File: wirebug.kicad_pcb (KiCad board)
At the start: 2 copper layers, 35 x 65 mm, 11 parts, among them J1 Screw_Terminal_01x02, J2 Screw_Terminal_01x02, J3 Screw_Terminal_01x02, K1 AW3211F, Q1 BC337, Q2 BC337

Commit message: RC1
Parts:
- added REF**: via_0.9, twyleg-misc:via_0.9, F.Cu at (120.9, 55.6)
- R1, R2: footprint Resistor_THT:R_Axial_DIN0204_L3.6mm_D1.6mm_P2.54mm_Vertical -> Resistor_THT:R_Axial_DIN0207_L6.3mm_D2.5mm_P2.54mm_Vertical
- moved Q1 2.72 mm to (110.9, 79.0), turned to -90 degrees
- moved Q2 2.68 mm to (117.9, 79.0), turned to -90 degrees
- moved PS1 2.55 mm to (121.3, 71.8)
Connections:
- A1 pad 13: unconnected-(A1-GND-Pad13) -> /GND
- A1 pad 18: unconnected-(A1-GND-Pad18) -> /GND
- A1 pad 23: unconnected-(A1-GND-Pad23) -> /GND
- A1 pad 28: unconnected-(A1-GND-Pad28) -> /GND
- A1 pad 3: unconnected-(A1-GND-Pad3) -> /GND
- A1 pad 33: unconnected-(A1-GND|AGND-Pad33) -> /GND
- A1 pad 8: unconnected-(A1-GND-Pad8) -> /GND
- J1 pad 1: unconnected-(J1-Pin_1-Pad1) -> /SIG_IN
- J1 pad 2: unconnected-(J1-Pin_2-Pad2) -> /SIG_IN
- J2 pad 1: unconnected-(J2-Pin_1-Pad1) -> /SIG_OUT
- J2 pad 2: unconnected-(J2-Pin_2-Pad2) -> /SIG_OUT
- J3 pad 1: unconnected-(J3-Pin_1-Pad1) -> /VIN
- J3 pad 2: unconnected-(J3-Pin_2-Pad2) -> /GND
- K1 pad 3: unconnected-(K1-Pad3) -> /SIG_IN
- K1 pad 4: unconnected-(K1-Pad4) -> /SIG_OUT
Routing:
- net /3V3: track 0.00 -> 43.2 mm
- net /SIG_IN: track 0.00 -> 38.8 mm
- net /RESET: track 0.00 -> 35.8 mm
- net /SET: track 0.00 -> 29.0 mm
- net /SET_RELAY: track 0.00 -> 20.4 mm
- net /VIN: track 0.00 -> 11.5 mm
- net /SIG_OUT: track 0.00 -> 11.5 mm
- net Net-(Q1-B): track 0.00 -> 7.26 mm
- net /RESET_RELAY: track 0.00 -> 6.49 mm
- net Net-(Q2-B): track 0.00 -> 5.93 mm
- added copper zone on B.Cu, net /GND
- added copper zone on F.Cu, net /GND
- removed copper zone on B.Cu, net (none)
- removed copper zone on F.Cu, net (none)

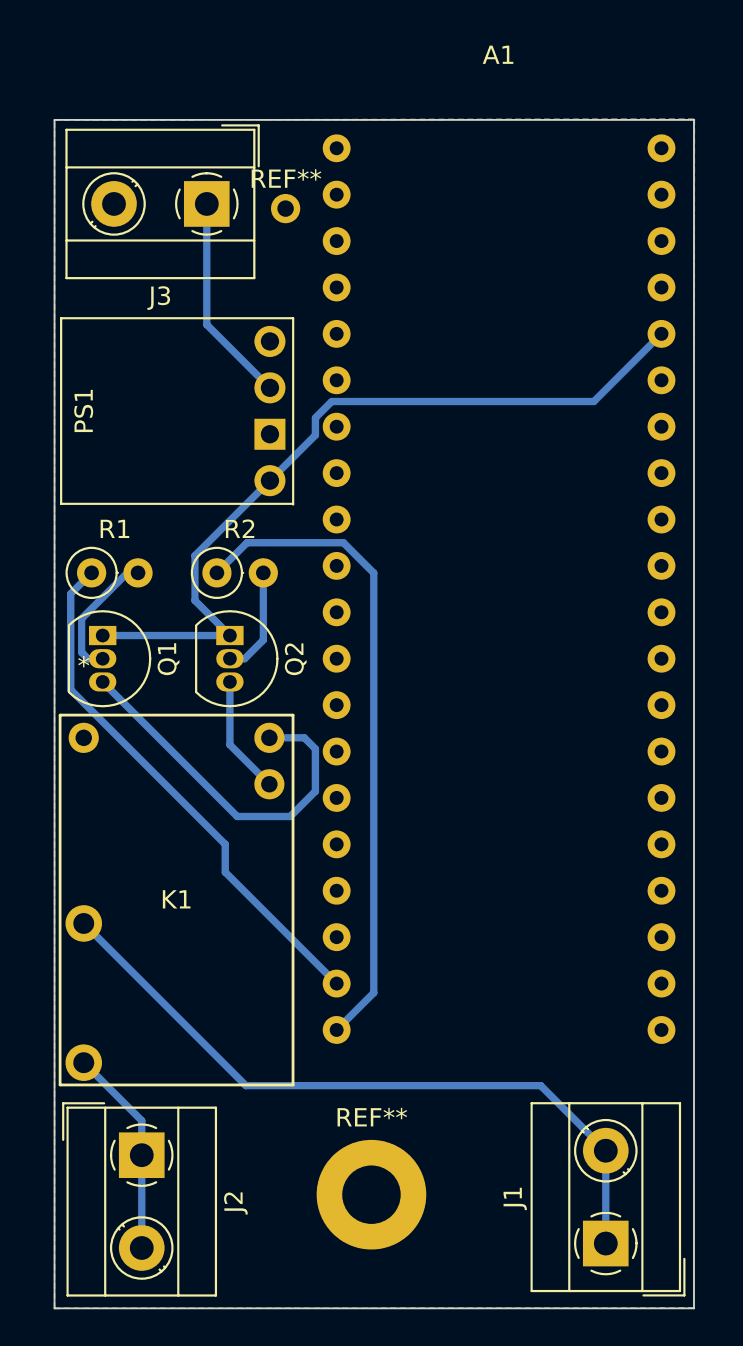
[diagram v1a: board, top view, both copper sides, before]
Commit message: Updated PicoW and voltage regultator
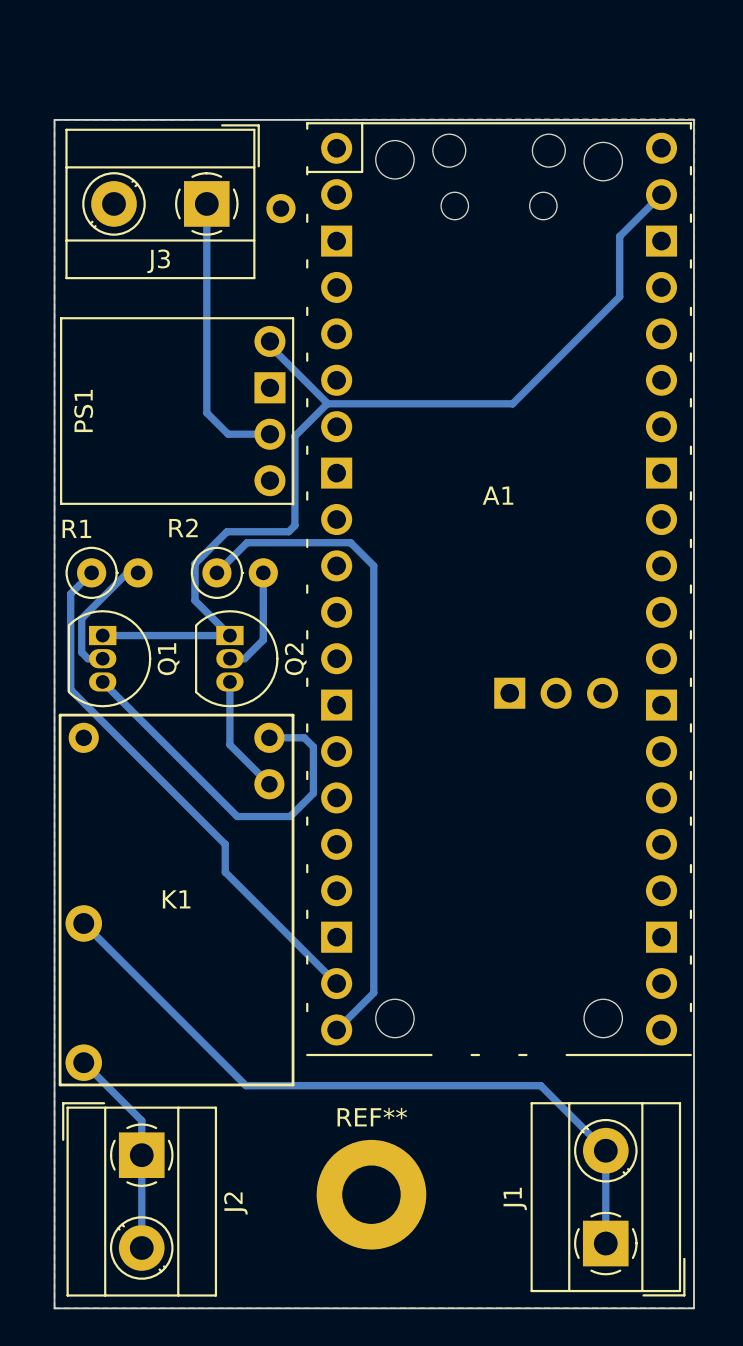
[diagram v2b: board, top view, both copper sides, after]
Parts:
- A1: footprint twyleg-board-connectors:RaspberryPiPico-THT-Dev -> twyleg-board-connectors:RaspberryPiPicoW-THT-Dev_No-SMT
- moved A1 24.1 mm to (132.6, 76.5)
- moved REF** 0.25 mm to (120.7, 55.6)
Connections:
- A1 pad 36: /3V3 -> unconnected-(A1-3V3(OUT)-Pad36)
- A1 pad 39: unconnected-(A1-VSYS-Pad39) -> /3V3
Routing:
- net /3V3: track 43.2 -> 55.1 mm
- net /VIN: track 11.5 -> 15.4 mm

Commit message: Smaller changes
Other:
- board size 35 x 65 mm -> 35.6 x 65.7 mm
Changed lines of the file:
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@@
     )
   )
-  (gr_rect (start 108.256 50.772) (end 143.256 115.8214)
+  (gr_rect (start 108.256 50.137) (end 143.891 115.8214)
     (stroke (width 0.1) (type default)) (fill none) (layer "Edge.Cuts"))
   (segment (start 134.869 103.632) (end 138.43 107.193) (width 0.4) (layer "B.Cu") (net 3))
@@
     (polygon
       (pts
-        (xy 108.2548 50.7746)
-        (xy 143.2814 50.7238)
-        (xy 143.256 115.7986)
+        (xy 108.2548 50.1396)
+        (xy 143.9164 50.0888)
+        (xy 143.891 115.7986)
         (xy 108.2548 115.824)
       )
